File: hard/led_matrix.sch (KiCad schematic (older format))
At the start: 0 parts

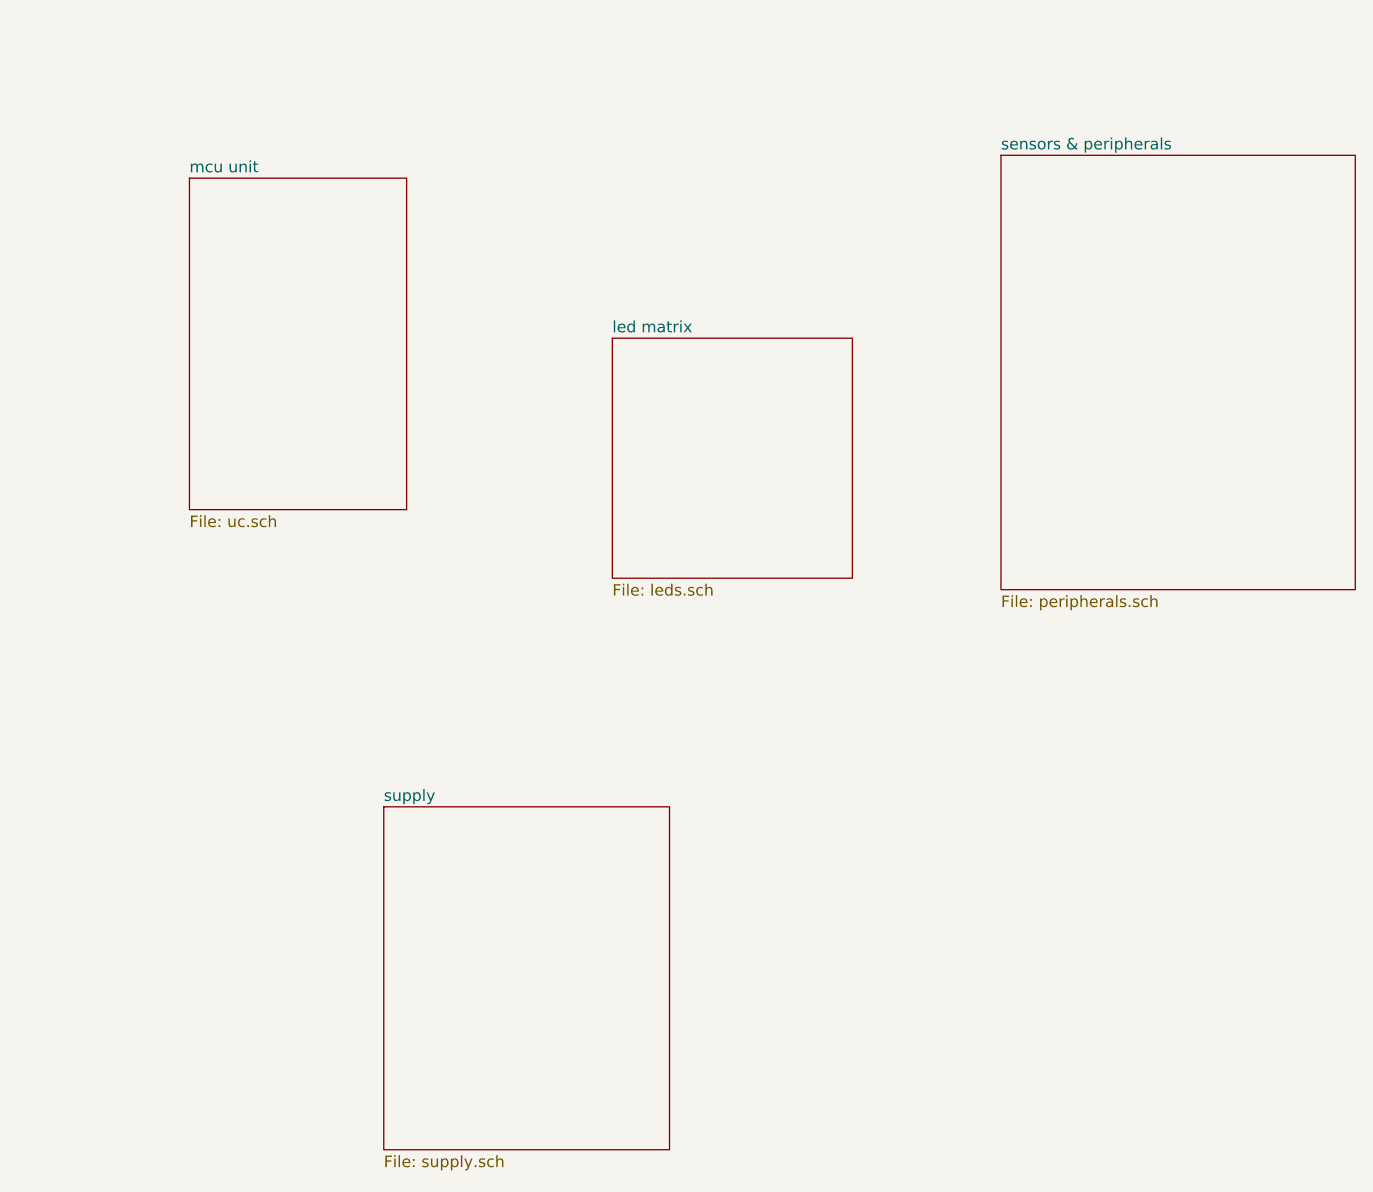
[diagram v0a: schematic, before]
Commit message: added various devices
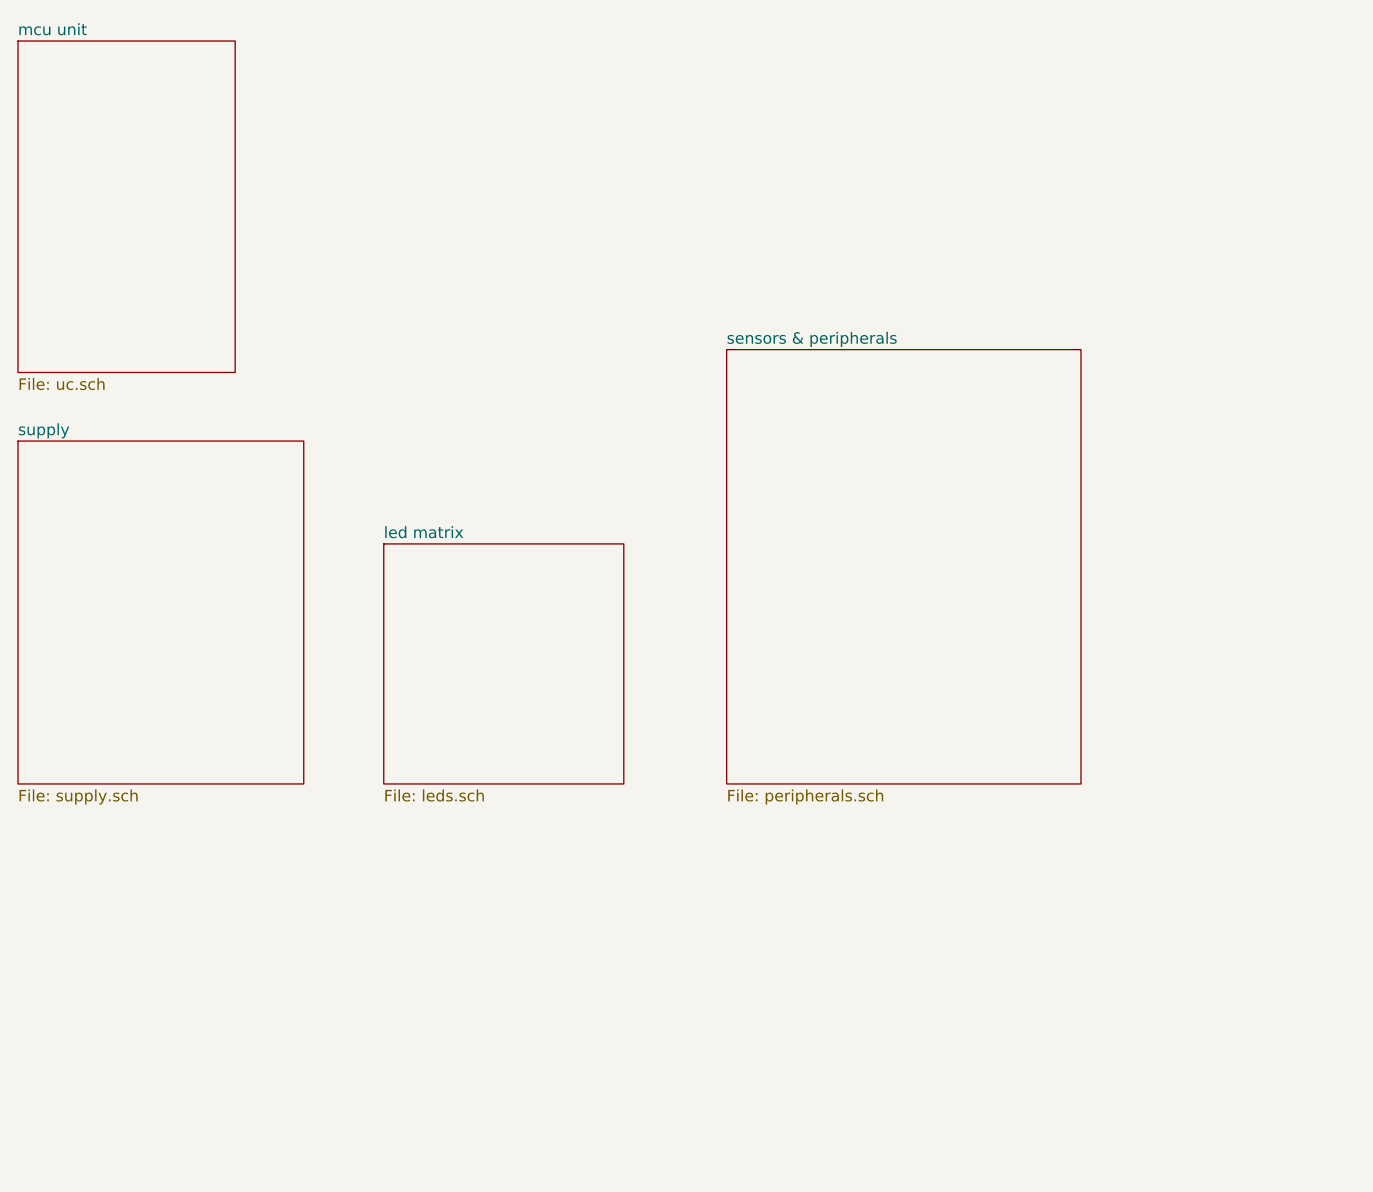
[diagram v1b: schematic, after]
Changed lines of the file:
@@
 $EndDescr
 $Sheet
-S 2150 1850 950  1450
+S 1400 1250 950  1450
 U 6053C560
 F0 "mcu unit" 50
@@
 $EndSheet
 $Sheet
-S 4000 2550 1050 1050
+S 3000 3450 1050 1050
 U 6053C67A
 F0 "led matrix" 50
@@
 $EndSheet
 $Sheet
-S 3000 4600 1250 1500
+S 1400 3000 1250 1500
 U 6053C80F
 F0 "supply" 50
@@
 $EndSheet
 $Sheet
-S 5700 1750 1550 1900
+S 4500 2600 1550 1900
 U 6053C8CB
 F0 "sensors & peripherals" 50

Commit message: release candidate. ready for review by @lukekaese
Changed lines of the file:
@@
 $Descr A4 11693 8268
 encoding utf-8
-Sheet 1 69
-Title ""
-Date ""
-Rev ""
-Comp ""
+Sheet 1 70
+Title "LED Matrix V3"
+Date "2021-03-23"
+Rev "0"
+Comp "F2A"
 Comment1 ""
 Comment2 ""
@@
 $EndDescr
 $Sheet
-S 1400 1250 950  1450
+S 2550 4150 1000 500
 U 6053C560
-F0 "mcu unit" 50
+F0 "MCU Unit" 197
 F1 "uc.sch" 50
 $EndSheet
 $Sheet
-S 3000 3450 1050 1050
+S 2550 2150 1000 500
 U 6053C67A
-F0 "led matrix" 50
+F0 "LED Matrix" 197
 F1 "leds.sch" 50
 $EndSheet
 $Sheet
-S 1400 3000 1250 1500
+S 2550 3150 1000 500
 U 6053C80F
-F0 "supply" 50
+F0 "Supply" 197
 F1 "supply.sch" 50
 $EndSheet
 $Sheet
-S 4500 2600 1550 1900
+S 2550 5150 1000 500
 U 6053C8CB
-F0 "sensors & peripherals" 50
+F0 "Sensors & Peripherals" 197
 F1 "peripherals.sch" 50
 $EndSheet
